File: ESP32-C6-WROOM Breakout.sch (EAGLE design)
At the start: 85 parts, among them J1 HP I2C, J11 LP I2C, J12 UART Vcc, J14 I_measure, J2 HP I2C, J3 HP_UART, P1 LP_I2C, P10 Pwr Sw 23, P11 Battery, P12 Pwr Out, P13 Pwr Sw 22, P14 Backup, P2 HP_I2C, P3 CTRL, P4 HI DRV/CNT, P5 ADC (ext batt), P6 GPIO-A1, P7 HP_UART, P8 GPIO-A2, P9 GPIO-B, Q1 FDN338P, Q2 FDN338P, Q3 FDN338P, U1 74LVC1G3157, U2 ESP32-C6-WROOM-1-N4LONG, U3 RT9080-33, U4 MIC2005A-1YM5, U5 MIC2005A-1YM5, X1 CFS-20632768EZFB

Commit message: prepared for panelisation process
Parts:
- renumbered JP1 to J15, JP11 to J19, JP2 to J16, JP3 to J17, JP5 to J18
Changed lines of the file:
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@@
 <part name="R8" library="Master 2016" deviceset="R-EU_" device="" value="10k"/>
 <part name="SUPPLY5" library="Master 2016" deviceset="VCC" device=""/>
-<part name="JP5" library="Master 2016" deviceset="HEADER-1X2P" device="PTH"/>
+<part name="J18" library="Master 2016" deviceset="HEADER-1X2P" device="PTH"/>
 <part name="R1" library="Master 2016" deviceset="R-EU_" device=""/>
 <part name="R10" library="Master 2016" deviceset="R-EU_" device="" value="3k3"/>
@@
 <part name="GND4" library="Master 2016" deviceset="GND" device=""/>
 <part name="GND5" library="Master 2016" deviceset="GND" device=""/>
-<part name="JP1" library="Master 2016" deviceset="HEADER-1X2P" device="PTH"/>
-<part name="JP2" library="Master 2016" deviceset="HEADER-1X2P" device="PTH"/>
+<part name="J15" library="Master 2016" deviceset="HEADER-1X2P" device="PTH"/>
+<part name="J16" library="Master 2016" deviceset="HEADER-1X2P" device="PTH"/>
 <part name="GND6" library="Master 2016" deviceset="GND" device=""/>
 <part name="J14" library="Master 2016" deviceset="HEADER-1X2P" device="PTH" value="I_measure"/>
-<part name="JP3" library="Master 2016" deviceset="HEADER-1X2P" device="PTH" value="BOOT"/>
+<part name="J17" library="Master 2016" deviceset="HEADER-1X2P" device="PTH" value="BOOT"/>
 <part name="GND7" library="Master 2016" deviceset="GND" device=""/>
 <part name="R9" library="Master 2016" deviceset="R-EU_" device="" value="470"/>
@@
 <part name="LED2" library="Master 2016" deviceset="LED" device="1206"/>
 <part name="R2" library="Master 2016" deviceset="R-EU_" device=""/>
-<part name="JP11" library="Master 2016" deviceset="HEADER-1X2P" device="PTH"/>
+<part name="J19" library="Master 2016" deviceset="HEADER-1X2P" device="PTH"/>
 <part name="C5" library="Master 2016" deviceset="CPOL-EU" device="E2.5-5**10UF" value="1u"/>
 <part name="C7" library="Master 2016" deviceset="C-EU" device="1206" value="1u"/>
@@
 <attribute name="VALUE" x="164.084" y="67.056" size="1.778" layer="96"/>
 </instance>
-<instance part="JP5" gate="G$1" x="190.5" y="53.34" smashed="yes" rot="R180">
+<instance part="J18" gate="G$1" x="190.5" y="53.34" smashed="yes" rot="R180">
 <attribute name="VALUE" x="193.04" y="58.42" size="1.778" layer="96" rot="R180"/>
 <attribute name="NAME" x="191.77" y="58.928" size="1.778" layer="95" rot="R180"/>
@@
 <attribute name="VALUE" x="170.18" y="33.02" size="1.778" layer="96"/>
 </instance>
-<instance part="JP1" gate="G$1" x="-35.56" y="-22.86" smashed="yes" rot="R180">
+<instance part="J15" gate="G$1" x="-35.56" y="-22.86" smashed="yes" rot="R180">
 <attribute name="VALUE" x="-33.02" y="-17.78" size="1.778" layer="96" rot="R180"/>
 <attribute name="NAME" x="-33.02" y="-28.702" size="1.778" layer="95" rot="R180"/>
 </instance>
-<instance part="JP2" gate="G$1" x="-12.7" y="-22.86" smashed="yes" rot="R180">
+<instance part="J16" gate="G$1" x="-12.7" y="-22.86" smashed="yes" rot="R180">
 <attribute name="VALUE" x="-10.16" y="-17.78" size="1.778" layer="96" rot="R180"/>
 <attribute name="NAME" x="-10.16" y="-28.702" size="1.778" layer="95" rot="R180"/>
@@
 <attribute name="NAME" x="8.382" y="78.74" size="1.778" layer="95" rot="R270"/>
 </instance>
-<instance part="JP3" gate="G$1" x="-35.56" y="-2.54" smashed="yes" rot="R180">
+<instance part="J17" gate="G$1" x="-35.56" y="-2.54" smashed="yes" rot="R180">
 <attribute name="VALUE" x="-33.02" y="2.54" size="1.778" layer="96" rot="R180"/>
 <attribute name="NAME" x="-33.02" y="-8.382" size="1.778" layer="95" rot="R180"/>
@@
 <attribute name="VALUE" x="34.29" y="-5.842" size="1.778" layer="96"/>
 </instance>
-<instance part="JP11" gate="G$1" x="48.26" y="-10.16" smashed="yes" rot="R90">
+<instance part="J19" gate="G$1" x="48.26" y="-10.16" smashed="yes" rot="R90">
 <attribute name="VALUE" x="53.34" y="-12.7" size="1.778" layer="96" rot="R90"/>
 <attribute name="NAME" x="42.418" y="-12.7" size="1.778" layer="95" rot="R90"/>
@@
 </segment>
 <segment>
-<pinref part="JP1" gate="G$1" pin="2"/>
+<pinref part="J15" gate="G$1" pin="2"/>
 <wire x1="-43.18" y1="-25.4" x2="-43.18" y2="-33.02" width="0.1524" layer="91"/>
 <wire x1="-43.18" y1="-33.02" x2="-20.32" y2="-33.02" width="0.1524" layer="91"/>
 <wire x1="-20.32" y1="-33.02" x2="7.62" y2="-33.02" width="0.1524" layer="91"/>
-<pinref part="JP2" gate="G$1" pin="2"/>
+<pinref part="J16" gate="G$1" pin="2"/>
 <wire x1="-20.32" y1="-25.4" x2="-20.32" y2="-33.02" width="0.1524" layer="91"/>
 <junction x="-20.32" y="-33.02"/>
@@
 <segment>
 <wire x1="-45.72" y1="-7.62" x2="-45.72" y2="-5.08" width="0.1524" layer="91"/>
-<pinref part="JP3" gate="G$1" pin="2"/>
+<pinref part="J17" gate="G$1" pin="2"/>
 <wire x1="-45.72" y1="-5.08" x2="-43.18" y2="-5.08" width="0.1524" layer="91"/>
 <pinref part="GND7" gate="1" pin="GND"/>
@@
 <pinref part="Q1" gate="MOS" pin="S"/>
 <wire x1="172.72" y1="63.5" x2="172.72" y2="53.34" width="0.1524" layer="91"/>
-<pinref part="JP5" gate="G$1" pin="1"/>
+<pinref part="J18" gate="G$1" pin="1"/>
 <wire x1="172.72" y1="53.34" x2="172.72" y2="50.8" width="0.1524" layer="91"/>
 <wire x1="182.88" y1="53.34" x2="172.72" y2="53.34" width="0.1524" layer="91"/>
@@
 <net name="N$1" class="0">
 <segment>
-<pinref part="JP3" gate="G$1" pin="1"/>
+<pinref part="J17" gate="G$1" pin="1"/>
 <wire x1="-43.18" y1="-2.54" x2="-45.72" y2="-2.54" width="0.1524" layer="91"/>
 <pinref part="R9" gate="G$1" pin="1"/>
@@
 <segment>
 <pinref part="R2" gate="G$1" pin="2"/>
-<pinref part="JP11" gate="G$1" pin="2"/>
+<pinref part="J19" gate="G$1" pin="2"/>
 <wire x1="43.18" y1="-2.54" x2="45.72" y2="-2.54" width="0.1524" layer="91"/>
 </segment>
@@
 <net name="N$11" class="0">
 <segment>
-<pinref part="JP11" gate="G$1" pin="1"/>
+<pinref part="J19" gate="G$1" pin="1"/>
 <pinref part="LED2" gate="G$1" pin="A"/>
 <wire x1="48.26" y1="-2.54" x2="50.8" y2="-2.54" width="0.1524" layer="91"/>
@@
 <net name="N$9" class="0">
 <segment>
-<pinref part="JP2" gate="G$1" pin="1"/>
+<pinref part="J16" gate="G$1" pin="1"/>
 <pinref part="J5" gate="G$1" pin="1"/>
 <wire x1="-20.32" y1="-22.86" x2="-27.94" y2="-22.86" width="0.1524" layer="91"/>
@@
 <net name="N$16" class="0">
 <segment>
-<pinref part="JP1" gate="G$1" pin="1"/>
+<pinref part="J15" gate="G$1" pin="1"/>
 <pinref part="J4" gate="G$1" pin="1"/>
 <wire x1="-43.18" y1="-22.86" x2="-50.8" y2="-22.86" width="0.1524" layer="91"/>
@@
 <wire x1="172.72" y1="40.64" x2="180.34" y2="40.64" width="0.1524" layer="91"/>
 <wire x1="180.34" y1="40.64" x2="180.34" y2="50.8" width="0.1524" layer="91"/>
-<pinref part="JP5" gate="G$1" pin="2"/>
+<pinref part="J18" gate="G$1" pin="2"/>
 <wire x1="180.34" y1="50.8" x2="182.88" y2="50.8" width="0.1524" layer="91"/>
 <pinref part="P10" gate="G$1" pin="2"/>

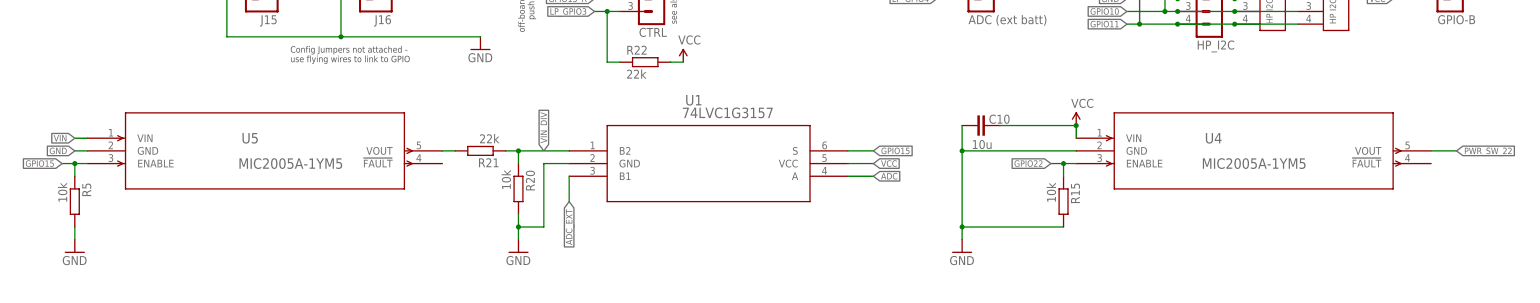
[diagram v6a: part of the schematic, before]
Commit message: minor tweaks with no electrical effect
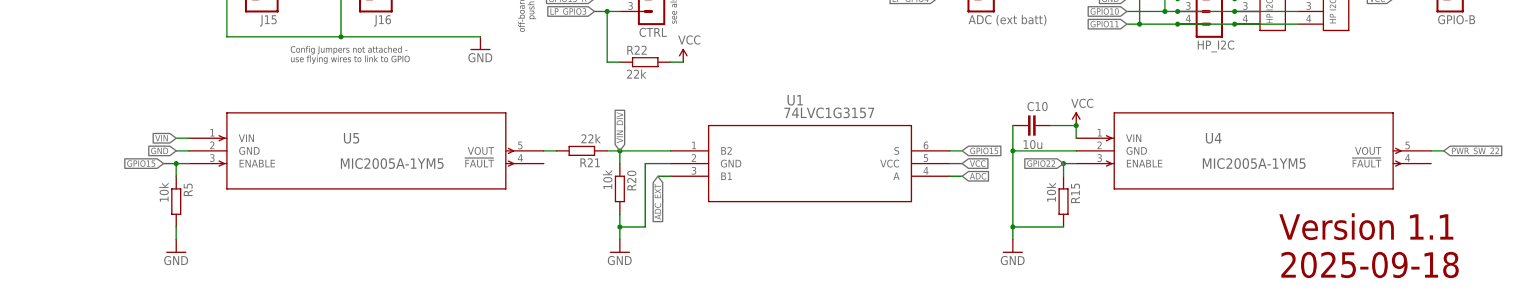
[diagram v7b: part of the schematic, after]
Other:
- note added: "Version 1.1 2025-09-18"
- moved on the sheet: C10, R20, R21, R5, U1, U5
